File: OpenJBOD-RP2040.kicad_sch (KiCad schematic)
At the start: 58 parts, among them J1 ATX-24, J2 Bus_PCI_Express_x1, J3 Conn_02x02_Counter_Clockwise, J4 UART, J8 USB_B_Micro, J9 TEMP1, Q1 MMBT3904, Q2 MMBT3904, SW1 SW_Push, SW2 TC-6615-6-260G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

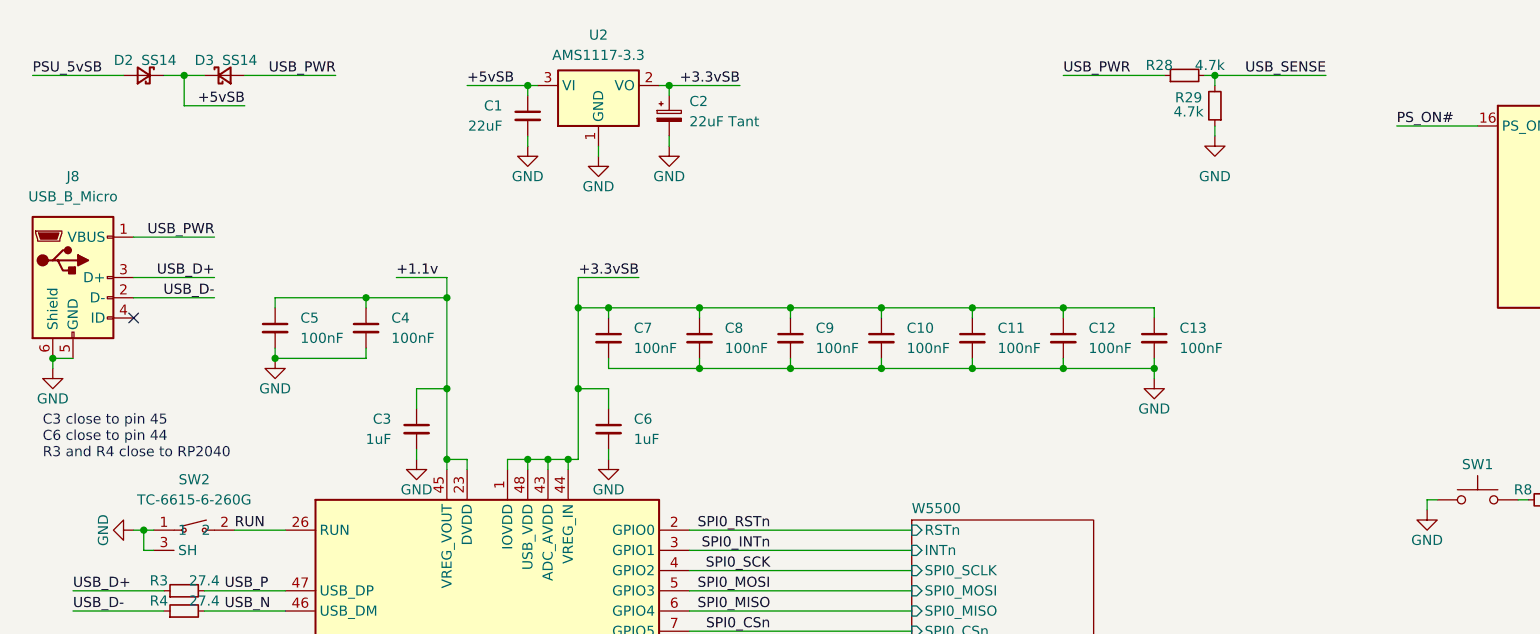
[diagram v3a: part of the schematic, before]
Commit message: replace USB micro B with USB C, requires cleanup
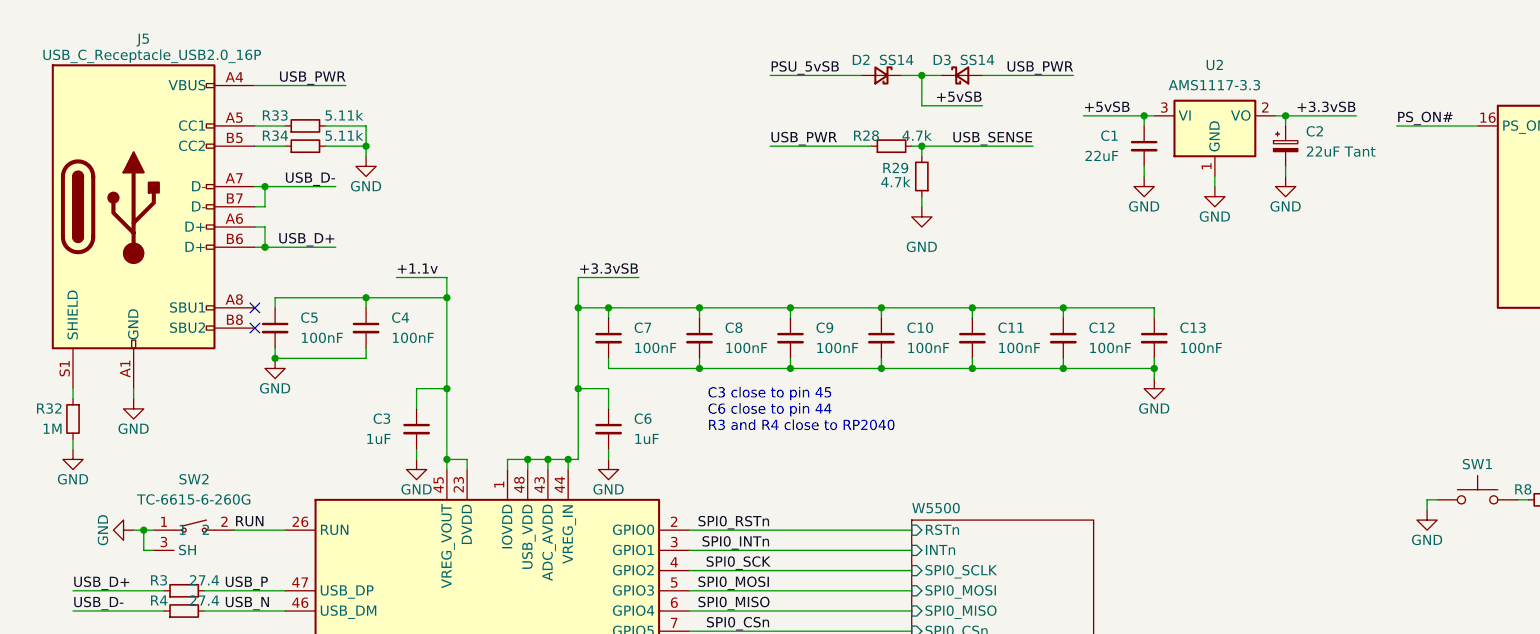
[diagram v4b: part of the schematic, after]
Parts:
- removed J8: USB_B_Micro, Connector_USB:USB_Micro-B_Amphenol_10118194_Horizontal, symbol Connector:USB_B_Micro
- added J5: USB_C_Receptacle_USB2.0_16P, OpenJBOD_Library:USB-C-SMD_TYPE-C-16PIN-2MD-073, symbol Connector:USB_C_Receptacle_USB2.0_16P
- added R32: 1M, Resistor_SMD:R_0402_1005Metric, symbol Device:R_Small
- added R33, R34: 5.11k, Resistor_SMD:R_1206_3216Metric, symbol Device:R_Small
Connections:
- net GND: now also J5.A1 (GND), J5.A12 (GND), J5.B1 (GND), J5.B12 (GND), R32.2, R33.2, R34.2
- net USB_D+: now also J5.A6 (D+), J5.B6 (D+)
- net USB_D-: now also J5.A7 (D-), J5.B7 (D-)
- net USB_PWR: now also J5.A4 (VBUS), J5.A9 (VBUS), J5.B4 (VBUS), J5.B9 (VBUS)
- new net: J5.A5 (CC1), R33.1
- new net: J5.B5 (CC2), R34.1
- new net: J5.S1 (SHIELD), R32.1
- no-connect marks 31 -> 32
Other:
- moved on the sheet: C1, C2, D2, D3, R28, R29, U2
